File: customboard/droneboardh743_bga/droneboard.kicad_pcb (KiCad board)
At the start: 4 copper layers, 38 x 38 mm, 68 parts, among them J1 Conn_01x04_MountingPin, J10 Conn_01x03_Pin, J2 Conn_01x04_MountingPin, J3 Conn_01x08_MountingPin, J4 Conn_01x08_MountingPin, J5 USB_C_Receptacle_USB2.0_16P, J6 Conn_01x06_MountingPin, J7 Conn_01x06_MountingPin, Q1 DMN3042L, SW1 434133025816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

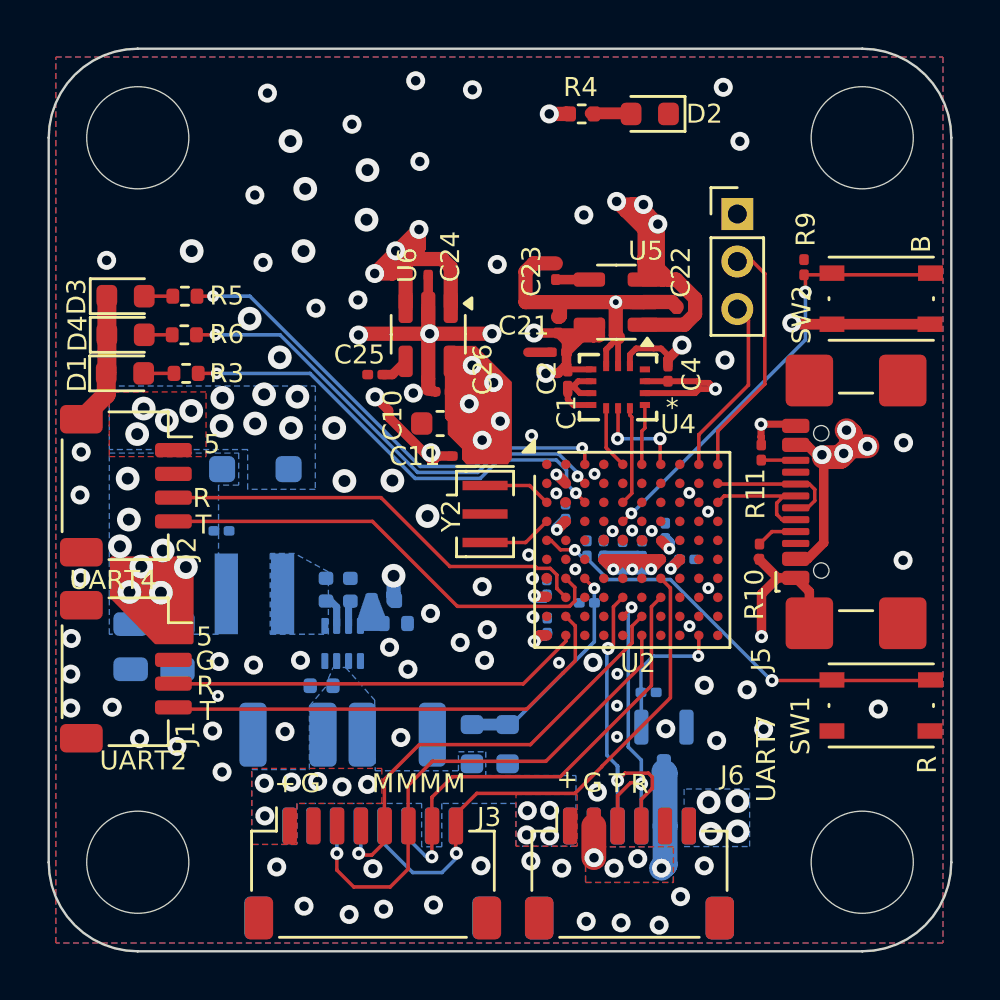
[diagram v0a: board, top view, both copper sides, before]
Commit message: HAL fixes, remove 5V diode
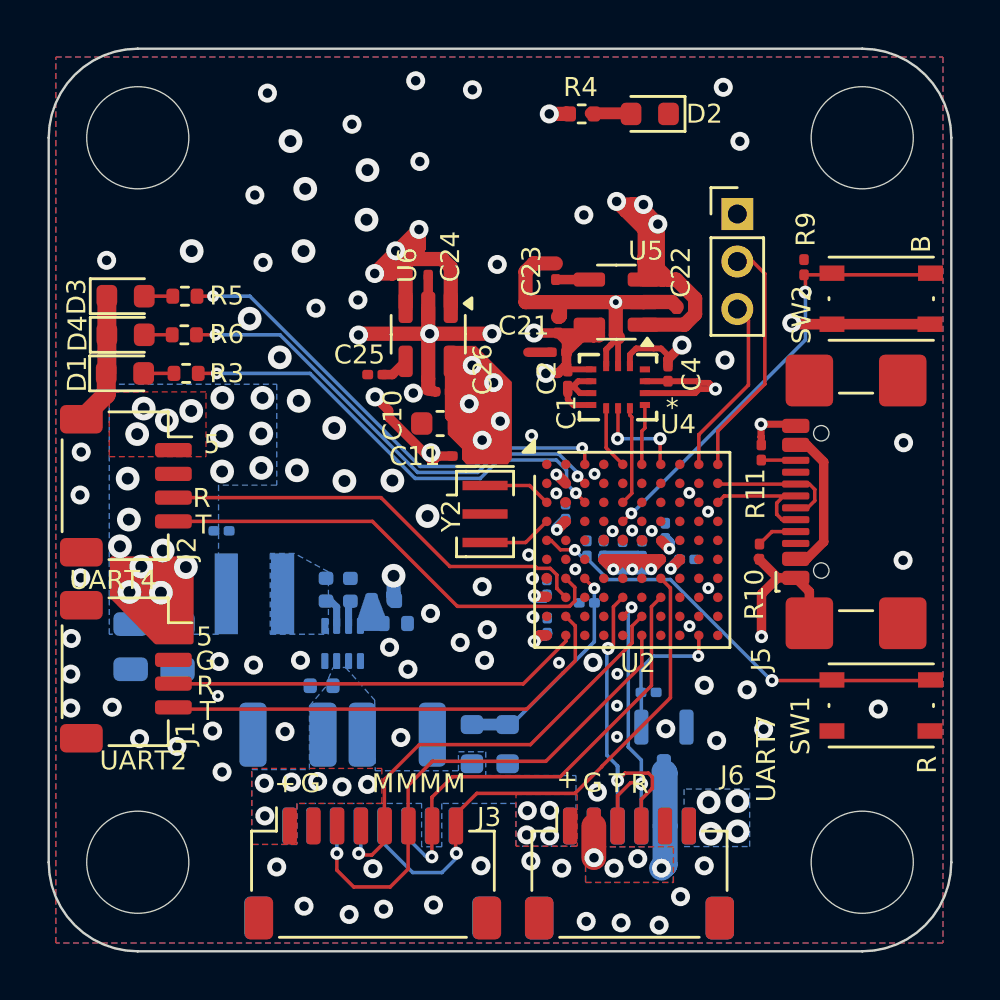
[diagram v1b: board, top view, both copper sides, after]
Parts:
- removed D5: MBR120VLSFT1G, Diode_SMD:D_SOD-123F
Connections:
- C22 pad 1: /VUSB -> /5V
- C24 pad 1: /VUSB -> /5V
- J2 pad 1: /VUSB -> /5V
- J5 pad A4: /VUSB -> /NOVBUS
- J5 pad A9: /VUSB -> /NOVBUS
- J5 pad B4: /VUSB -> /NOVBUS
- J5 pad B9: /VUSB -> /NOVBUS
- R4 pad 1: /VUSB -> /5V
- U5 pad 1: /VUSB -> /5V
- U5 pad 3: /VUSB -> /5V
- U6 pad 1: /VUSB -> /5V
- U6 pad 3: /VUSB -> /5V
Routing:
- net /VUSB: track 51.7 -> 0.00 mm, vias 21 -> 0
- net /5V: track 1.05 -> 43.2 mm, vias 13 -> 30
- net /NOVBUS: track 0.00 -> 6.32 mm
- net /GND: vias 103 -> 105
- added copper zone on F.Cu, net /5V
- removed copper zone on B.Cu, net /VUSB
- removed copper zone on F.Cu, net /VUSB
- removed copper zone on In2.Cu, net /VUSB
